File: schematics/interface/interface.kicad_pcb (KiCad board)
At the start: 2 copper layers, 9 parts, among them J3 Conn_02x25_Counter_Clockwise, U1 74LS00, U2 74LS02, U4 74LS245, U5 74LS193, U6 74LS193, U7 74LS193, U8 74LS193

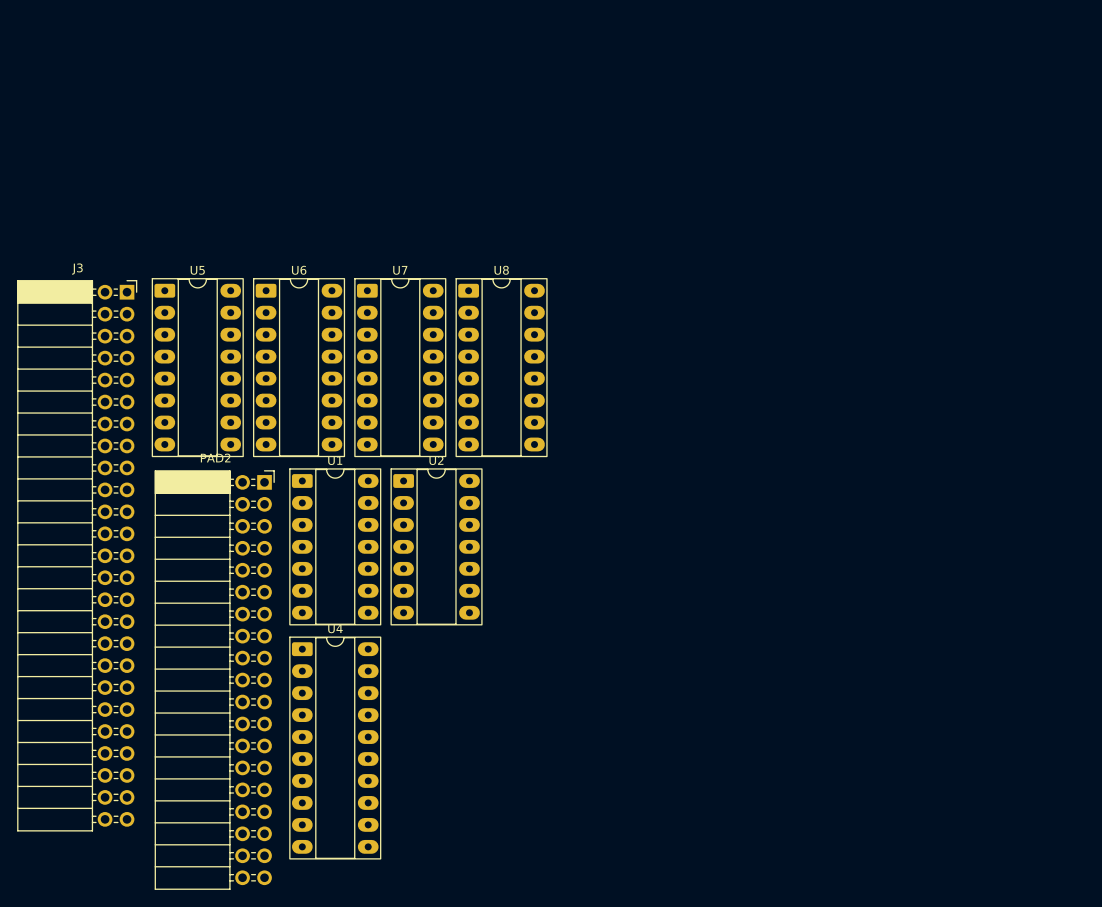
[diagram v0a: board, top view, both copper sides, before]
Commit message: structure(kicad): redefined the structure of the repository
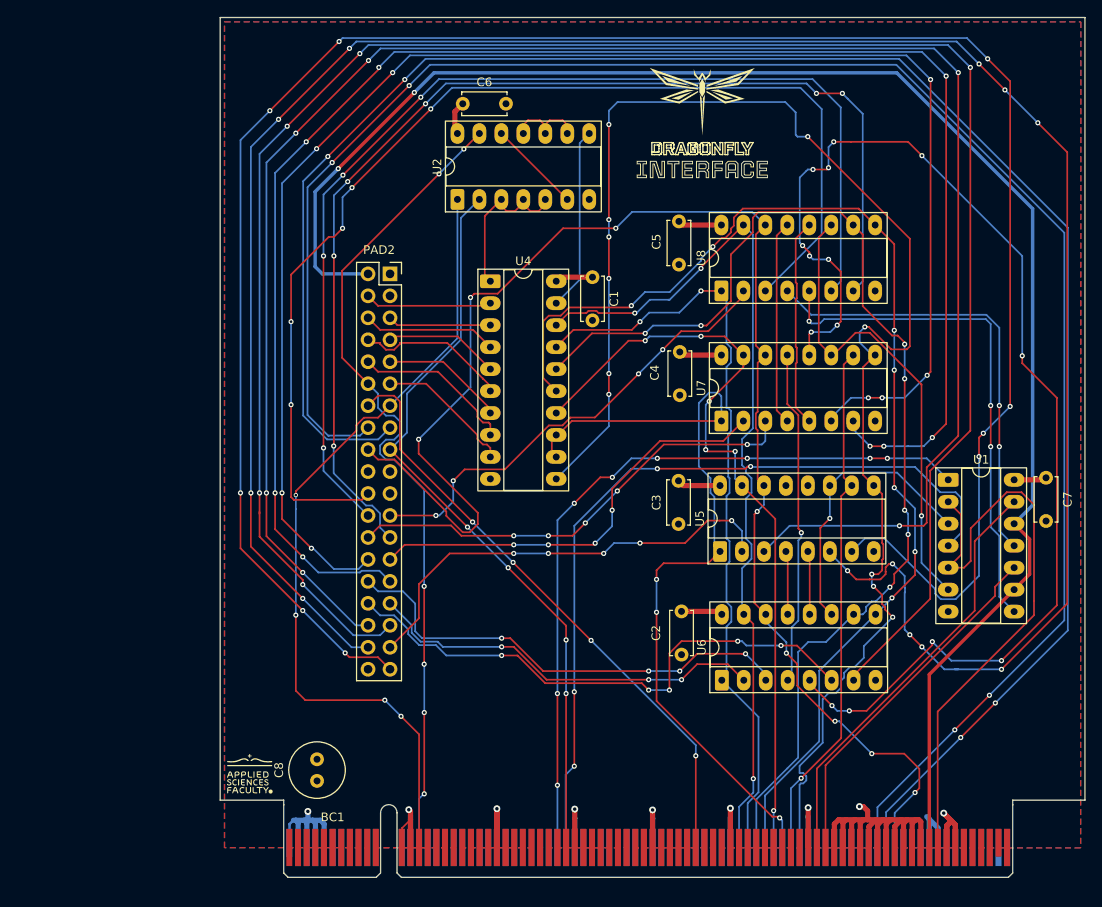
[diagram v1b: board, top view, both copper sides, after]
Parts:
- removed J3: Conn_02x25_Counter_Clockwise, Connector_PinSocket_2.54mm:PinSocket_2x25_P2.54mm_Horizontal
- added BC1: BusConnector, Connector_PCBEdge:BUS_PCIexpress_x16, F.Cu at (93.7, 118.6)
- added C1: C, Capacitor_THT:C_Disc_D5.0mm_W2.5mm_P5.00mm, F.Cu at (128.7, 52.6)
- added C2: C, Capacitor_THT:C_Disc_D5.0mm_W2.5mm_P5.00mm, F.Cu at (139.0, 91.3)
- added C3: C, Capacitor_THT:C_Disc_D5.0mm_W2.5mm_P5.00mm, F.Cu at (138.7, 76.2)
- added C4: C, Capacitor_THT:C_Disc_D5.0mm_W2.5mm_P5.00mm, F.Cu at (138.8, 61.3)
- added C5: C, Capacitor_THT:C_Disc_D5.0mm_W2.5mm_P5.00mm, F.Cu at (138.7, 46.2)
- added C6: C, Capacitor_THT:C_Disc_D5.0mm_W2.5mm_P5.00mm, F.Cu at (113.7, 32.6)
- added C7: C, Capacitor_THT:C_Disc_D5.0mm_W2.5mm_P5.00mm, F.Cu at (181.2, 75.8)
- added C8: C, Capacitor_THT:C_Radial_D6.3mm_H5.0mm_P2.50mm, F.Cu at (96.8, 110.9)
- added kibuzzard-6911D1BC: G***, kibuzzard-6911D1BC, F.Cu at (141.4, 40.2)
- PAD2: footprint Connector_PinSocket_2.54mm:PinSocket_2x19_P2.54mm_Horizontal -> Connector_PinSocket_2.54mm:PinSocket_2x19_P2.54mm_Vertical
- U2: value 74LS02 -> 74LS00
- moved U1 74.7 mm to (169.8, 76.1)
- moved U5 70.9 mm to (143.4, 84.4), turned to 90 degrees
- moved U6 69.3 mm to (143.7, 99.3), turned to 90 degrees
- moved U4 47.8 mm to (116.9, 53.1)
- moved U7 43.6 mm to (143.6, 69.3), turned to 90 degrees
- moved U2 33.1 mm to (113.1, 43.7), turned to 90 degrees
- moved U8 29.2 mm to (143.6, 54.2), turned to 90 degrees
- moved PAD2 28.1 mm to (105.3, 52.3)
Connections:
- PAD2 pad 12: /MemWrite -> /~{MemWrite}
- PAD2 pad 13: /MemRead -> /~{MemRead}
- PAD2 pad 14: /Halt -> /~{Halt}
- PAD2 pad 15: /Wait -> /~{Wait}
- PAD2 pad 17: /IntAck -> /~{IntAck}
- PAD2 pad 2: /Clk -> /~{Clk}
- U2 pad 1: Net-(U2-Pad1) -> /~{MemRead}
- U2 pad 12: Net-(U2-Pad10) -> Net-(U2-Pad12)
- U2 pad 13: Net-(U4-CE) -> /~{MemWrite}
- U2 pad 2: /MemRead -> /~{IntAck}
- U2 pad 3: /IntAck -> Net-(U4-A->B)
- U2 pad 5: Net-(U2-Pad1) -> Net-(U4-A->B)
- U2 pad 6: Net-(U2-Pad1) -> Net-(U2-Pad12)
- U2 pad 8: Net-(U4-A->B) -> Net-(U4-CE)
- U2 pad 9: /MemWrite -> Net-(U2-Pad10)
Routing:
- net /ADDRESS14: track 0.00 -> 264.3 mm, vias 0 -> 12
- net /ADDRESS15: track 0.00 -> 244.7 mm, vias 0 -> 9
- net /ADDRESS11: track 0.00 -> 230.0 mm, vias 0 -> 5
- net /~{Wait}: track 0.00 -> 221.6 mm, vias 0 -> 4
- net /ADDRESS12: track 0.00 -> 219.6 mm, vias 0 -> 6
- net /IntReq: track 0.00 -> 216.2 mm, vias 0 -> 4
- net /ADDRESS7: track 0.00 -> 195.6 mm, vias 0 -> 8
- net /~{Clk}: track 0.00 -> 190.6 mm, vias 0 -> 2
- net /ADDRESS6: track 0.00 -> 181.8 mm, vias 0 -> 8
- net /BUS7: track 0.00 -> 178.5 mm, vias 0 -> 11
- net /Reset: track 0.00 -> 173.6 mm, vias 0 -> 8
- net Net-(U6-UP): track 0.00 -> 140.1 mm, vias 0 -> 14
- net /BUS3: track 0.00 -> 135.3 mm, vias 0 -> 7
- net /ADDRESS0: track 0.00 -> 132.2 mm, vias 0 -> 5
- net /ADDRESS3: track 0.00 -> 131.6 mm, vias 0 -> 6
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- added copper zone on B.Cu, net GND
- added copper zone on F.Cu, net VCC
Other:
- board outline added: 100 x 91 mm

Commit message: silklayer check
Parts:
- moved C8 1.05 mm to (95.8, 110.8)
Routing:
- net VCC: track 51.7 -> 55.4 mm

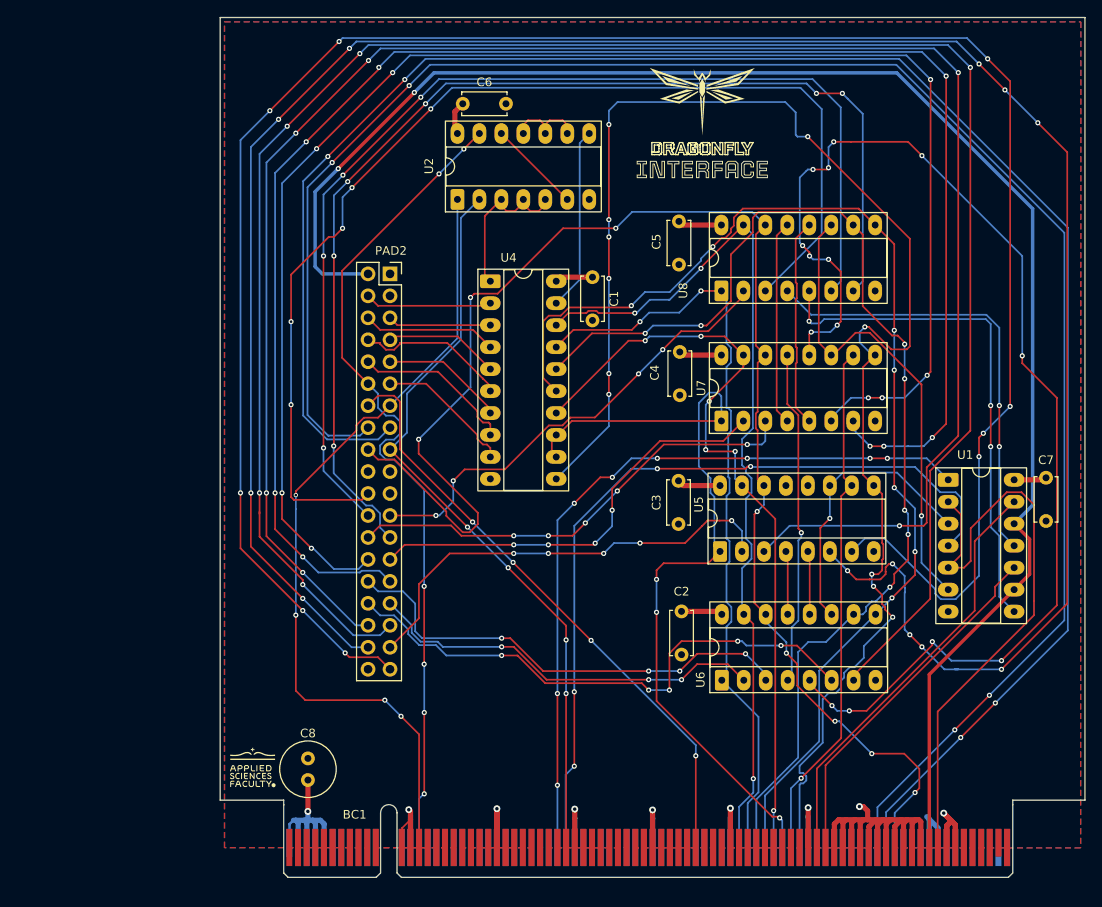
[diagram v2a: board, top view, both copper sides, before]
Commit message: fix(alu, core2, interface): vcc conection some routing issues
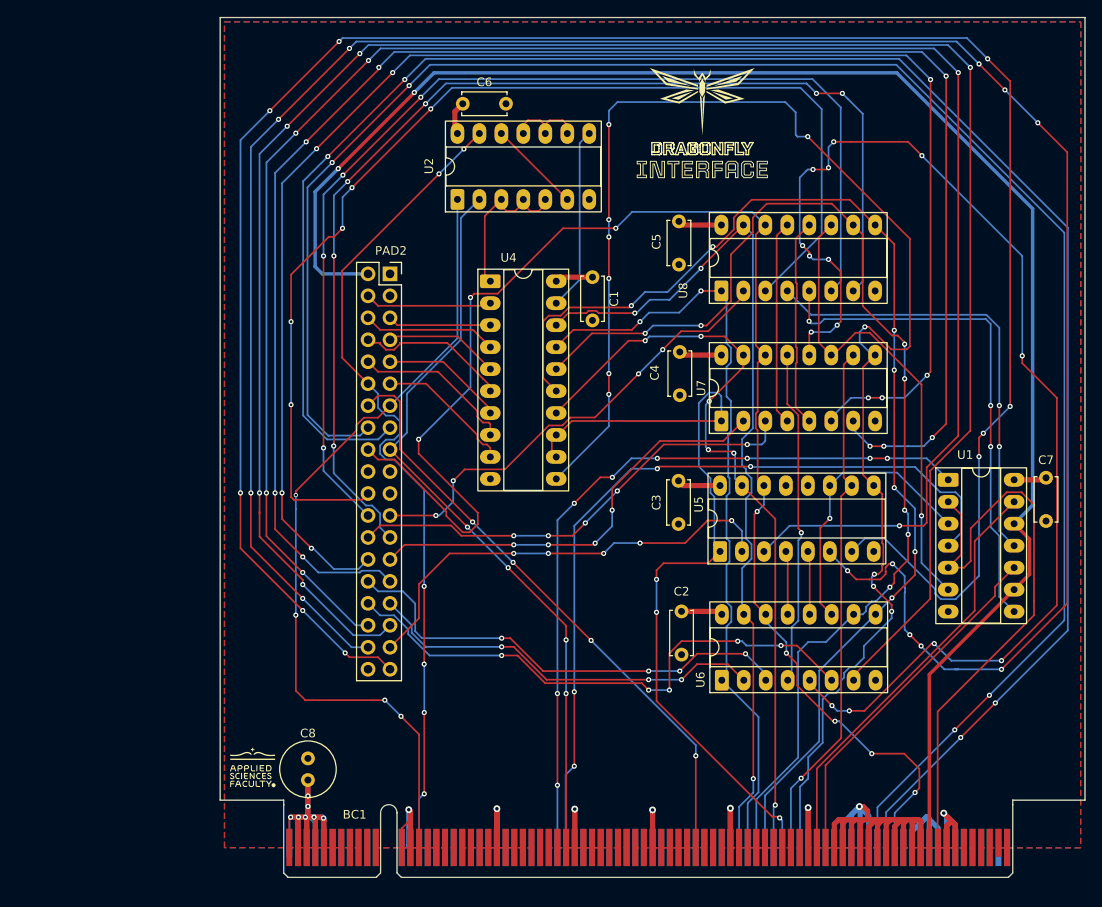
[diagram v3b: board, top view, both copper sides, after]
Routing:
- net GND: track 127.3 -> 170.5 mm
- net VCC: track 55.4 -> 83.0 mm, vias 1 -> 7
- net /BUS7: track 178.5 -> 177.2 mm
- net /BUS2: track 131.0 -> 131.8 mm
- net /BUS3: track 135.3 -> 136.0 mm

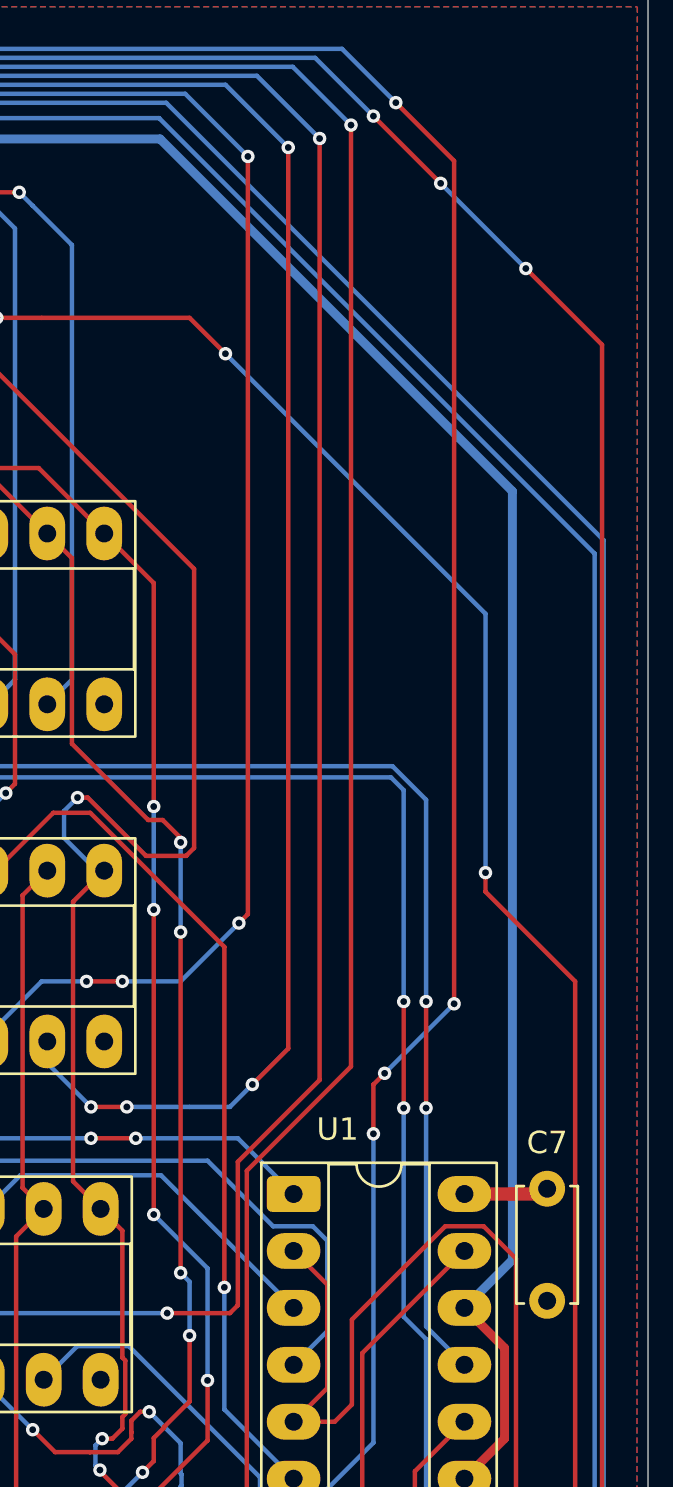
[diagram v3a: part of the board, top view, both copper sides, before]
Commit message: fix: removed in control pins daisy chains
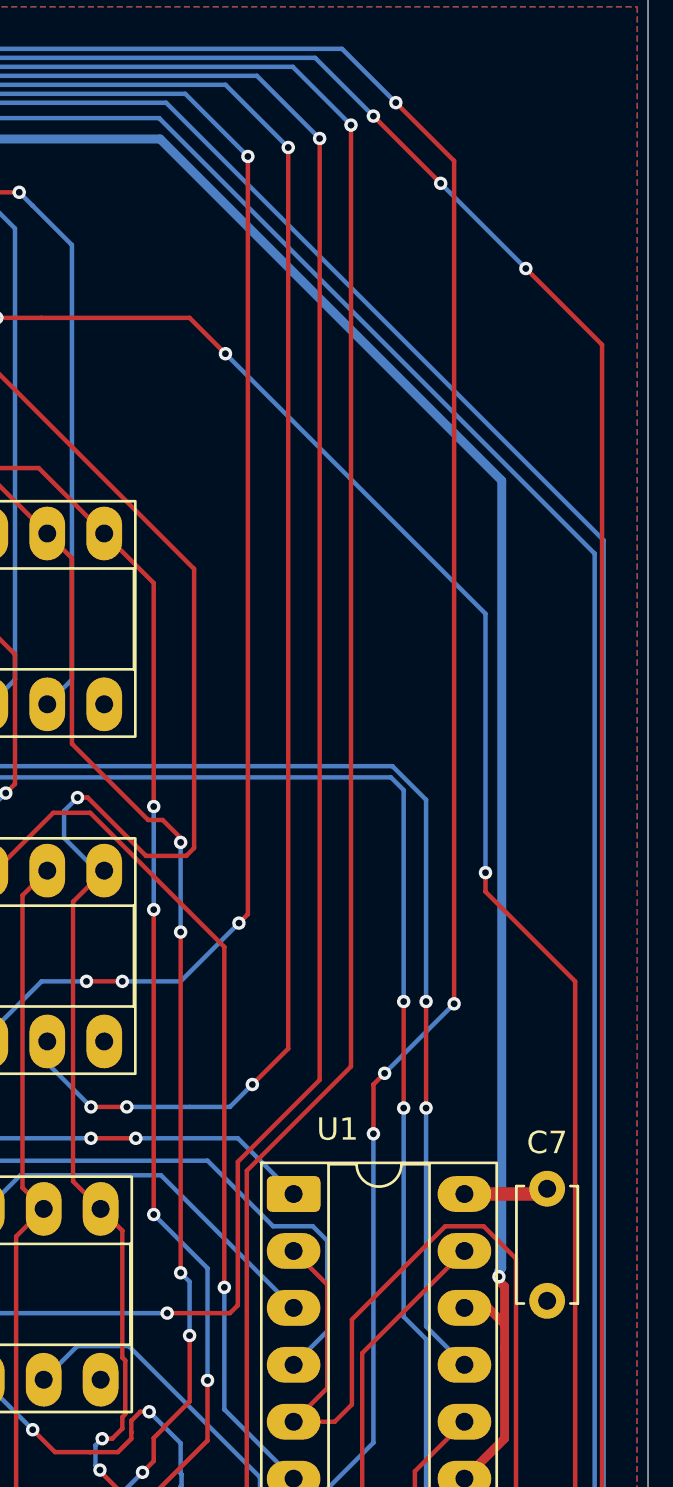
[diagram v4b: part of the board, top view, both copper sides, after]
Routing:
- net /~{Clk}: track 190.6 -> 191.0 mm, vias 2 -> 3
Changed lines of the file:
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@@
+	)
+	(segment
+		(start 179.25 80.215)
+		(end 179.25 81.9)
+		(width 0.4)
+		(layer "F.Cu")
+		(net 13)
 	)
 	(segment
@@
 	)
 	(segment
-		(start 179.25 82.955)
-		(end 177.46 81.165)
+		(start 179 79.965)
+		(end 179.25 80.215)
+		(width 0.4)
+		(layer "F.Cu")
+		(net 13)
+	)
+	(segment
+		(start 177.46 81.165)
+		(end 178.515 81.165)
+		(width 0.4)
+		(layer "F.Cu")
+		(net 13)
+	)
+	(segment
+		(start 179 79.775)
+		(end 179 79.965)
 		(width 0.4)
 		(layer "F.Cu")
@@
 		(net 13)
 	)
+	(segment
+		(start 178.515 81.165)
+		(end 179.25 81.9)
+		(width 0.4)
+		(layer "F.Cu")
+		(net 13)
+	)
+	(segment
+		(start 179.25 82.955)
+		(end 179.25 81.9)
+		(width 0.4)
+		(layer "F.Cu")
+		(net 13)
+	)
 	(via
 		(at 99.3 40.1)
+		(size 0.6)
+		(drill 0.3)
+		(layers "F.Cu" "B.Cu")
+		(net 13)
+	)
+	(via
+		(at 179 79.775)
 		(size 0.6)
 		(drill 0.3)
@@
 	)
 	(segment
-		(start 179.6 44.7371)
-		(end 163.8839 29.021)
-		(width 0.4)
-		(layer "B.Cu")
-		(net 13)
-	)
-	(segment
 		(start 97.47 52.27)
 		(end 102.75 52.27)
@@
 	)
 	(segment
-		(start 179.6 79.025)
-		(end 179.6 44.7371)
+		(start 179 79.775)
+		(end 179 79.515)
+		(width 0.4)
+		(layer "B.Cu")
+		(net 13)
+	)
+	(segment
+		(start 179 79.515)
+		(end 179.125 79.39)
+		(width 0.4)
+		(layer "B.Cu")
+		(net 13)
+	)
+	(segment
+		(start 179.125 44.2621)
+		(end 163.8839 29.021)
+		(width 0.4)
+		(layer "B.Cu")
+		(net 13)
+	)
+	(segment
+		(start 110.379 29.021)
+		(end 108.1 31.3)
 		(width 0.4)
 		(layer "B.Cu")
@@
 	)
 	(segment
-		(start 110.379 29.021)
-		(end 108.1 31.3)
+		(start 179.125 79.39)
+		(end 179.125 44.2621)
 		(width 0.4)
 		(layer "B.Cu")
@@
 		(width 0.4)
 		(layer "B.Cu")
-		(net 13)
-	)
-	(segment
-		(start 177.46 81.165)
-		(end 179.6 79.025)
-		(width 0.4)
-		(layer "B.Cu")

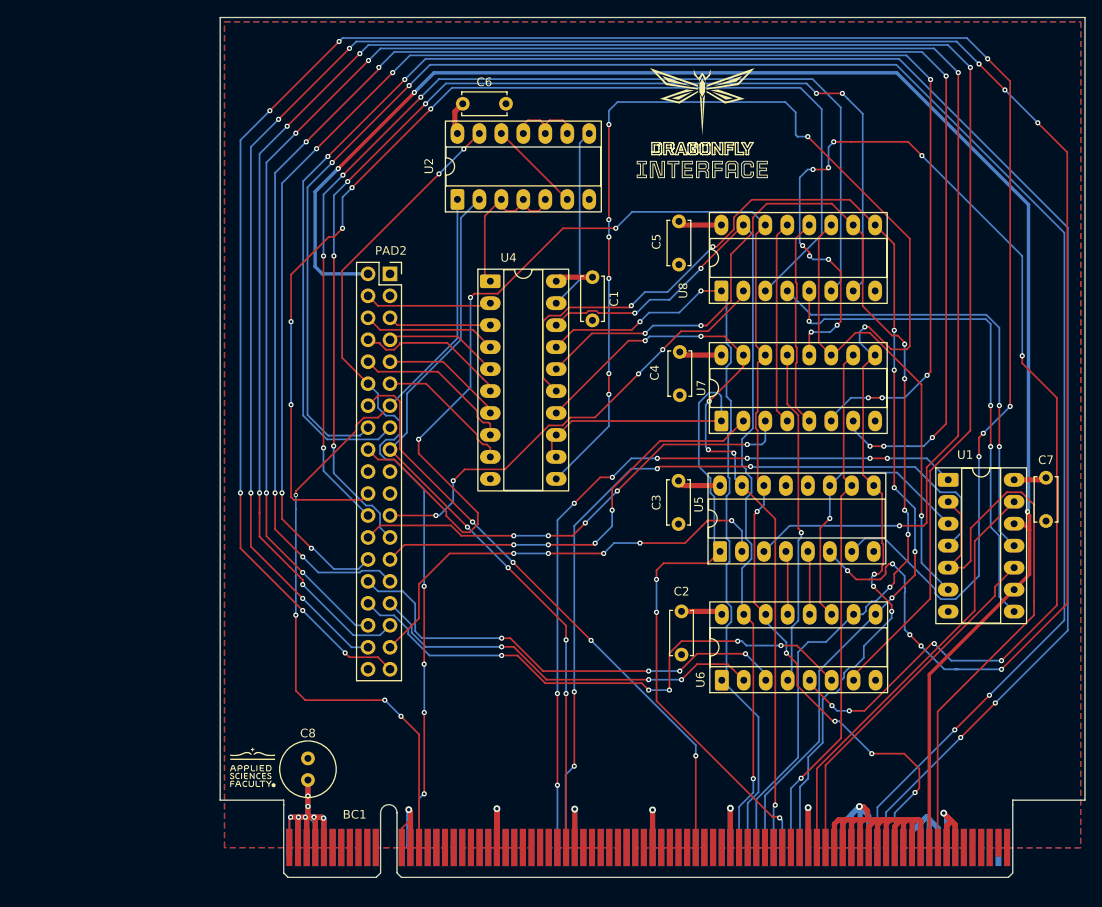
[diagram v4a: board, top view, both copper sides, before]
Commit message: fix(alu, core_1_2, interface): put vcc zones on back layer
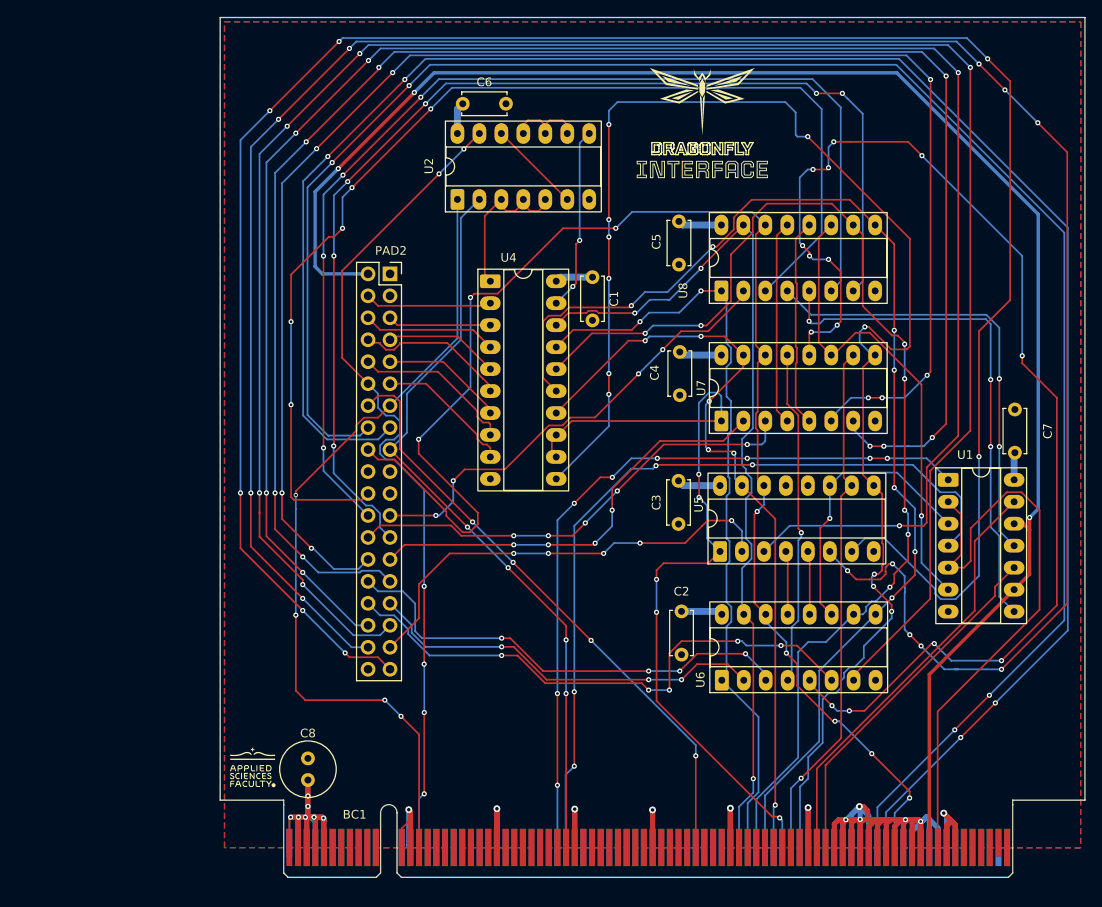
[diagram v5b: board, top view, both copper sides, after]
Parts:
- moved C7 4.62 mm to (177.6, 73.0), turned to 90 degrees
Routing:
- net /Reset: track 173.6 -> 170.5 mm
- net /~{Clk}: track 191.0 -> 191.7 mm
- net /Pulse: track 69.5 -> 70.0 mm
- net /BUS5: track 93.9 -> 94.0 mm, vias 3 -> 5
- net GND: vias 8 -> 12
- net /ADDRESS15: vias 9 -> 7
- net Net-(U4-CE): vias 0 -> 2
